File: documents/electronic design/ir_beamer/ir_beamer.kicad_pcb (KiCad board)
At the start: 2 copper layers, 140 parts, among them U1 74HC595D, U2 STM32F103HEADER, U3 74HC595D, U4 SE8R01_module

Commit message: update beamere pcb - MR_TOT in shift register, pull down
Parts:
- removed the C1 at (258.0, 110.3)
- removed the C1 at (233.8, 110.4)
- removed the C1 at (153.8, 110.4)
- removed the C1 at (179.3, 110.3)
- removed the C1 at (99.3, 110.3)
- removed the C1 at (73.8, 110.4)
- removed the C2 at (256.5, 25.0)
- removed the C2 at (235.4, 25.0)
- removed the C2 at (155.4, 25.0)
- removed the C2 at (177.7, 25.0)
- removed the C2 at (97.7, 25.0)
- removed the C2 at (75.4, 25.0)
- removed the C3 at (273.0, 38.2)
- removed the C3 at (218.8, 38.3)
- removed the C3 at (138.8, 38.3)
- removed the C3 at (194.3, 38.2)
- removed the C3 at (114.3, 38.2)
- removed the C3 at (58.8, 38.3)
- removed the D1 at (254.1, 74.0)
- removed the D1 at (237.7, 74.1)
- removed the D1 at (157.7, 74.1)
- removed the D1 at (175.4, 74.0)
- removed the D1 at (95.4, 74.0)
- removed the D1 at (77.7, 74.1)
- removed the D10 at (254.1, 61.3)
- removed the D10 at (237.7, 61.4)
- removed the D10 at (157.7, 61.4)
- removed the D10 at (175.4, 61.3)
- removed the D10 at (95.4, 61.3)
- removed the D10 at (77.7, 61.4)
- removed the D11 at (254.1, 67.6)
- removed the D11 at (237.7, 67.7)
- removed the D11 at (157.7, 67.7)
- removed the D11 at (175.4, 67.6)
- removed the D11 at (95.4, 67.6)
- removed the D11 at (77.7, 67.7)
- removed the D2 at (254.1, 42.2)
- removed the D2 at (237.7, 42.3)
- removed the D2 at (157.7, 42.3)
- removed the D2 at (175.4, 42.2)
- removed the D2 at (95.4, 42.2)
- removed the D2 at (77.7, 42.3)
- removed the D3 at (254.1, 80.3)
- removed the D3 at (237.7, 80.4)
- removed the D3 at (157.7, 80.4)
- removed the D3 at (175.4, 80.3)
- removed the D3 at (95.4, 80.3)
- removed the D3 at (77.7, 80.4)
- removed the D4 at (254.1, 86.7)
- removed the D4 at (237.7, 86.8)
- removed the D4 at (157.7, 86.8)
- removed the D4 at (175.4, 86.7)
- removed the D4 at (95.4, 86.7)
- removed the D4 at (77.7, 86.8)
- removed the D5 at (254.1, 93.0)
- removed the D5 at (237.7, 93.1)
- removed the D5 at (157.7, 93.1)
- removed the D5 at (175.4, 93.0)
- removed the D5 at (95.4, 93.0)
- removed the D5 at (77.7, 93.1)
- removed the D6 at (254.1, 99.4)
- removed the D6 at (237.7, 99.5)
- removed the D6 at (157.7, 99.5)
- removed the D6 at (175.4, 99.4)
- removed the D6 at (95.4, 99.4)
- removed the D6 at (77.7, 99.5)
- removed the D7 at (254.1, 105.7)
- removed the D7 at (237.7, 105.8)
- removed the D7 at (157.7, 105.8)
- removed the D7 at (175.4, 105.7)
- removed the D7 at (95.4, 105.7)
- removed the D7 at (77.7, 105.8)
- removed the D8 at (254.1, 48.6)
- removed the D8 at (237.7, 48.7)
- removed the D8 at (157.7, 48.7)
- removed the D8 at (175.4, 48.6)
- removed the D8 at (95.4, 48.6)
- removed the D8 at (77.7, 48.7)
- removed the D9 at (254.1, 54.9)
- removed the D9 at (237.7, 55.0)
- removed the D9 at (157.7, 55.0)
- removed the D9 at (175.4, 54.9)
- removed the D9 at (95.4, 54.9)
- removed the D9 at (77.7, 55.0)
- removed the R1 at (253.3, 111.1)
- removed the R1 at (238.6, 111.2)
- removed the R1 at (158.6, 111.2)
- removed the R1 at (174.5, 111.1)
- removed the R1 at (94.5, 111.1)
- removed the R1 at (78.6, 111.2)
- removed the R5 at (268.2, 86.4)
- removed the R5 at (223.7, 86.5)
- removed the R5 at (143.7, 86.5)
- removed the R5 at (189.4, 86.4)
- removed the R5 at (109.4, 86.4)
- removed the R5 at (63.7, 86.5)
- removed the U1 at (265.2, 105.0)
- removed the U1 at (226.6, 105.1)
- removed the U1 at (146.6, 105.1)
- removed the U1 at (186.4, 105.0)
- removed the U1 at (106.4, 105.0)
- removed the U1 at (66.6, 105.1)
- removed the U2 at (278.1, 96.7)
- removed the U2 at (213.7, 96.8)
- removed the U2 at (133.7, 96.8)
- removed the U2 at (199.4, 96.7)
- removed the U2 at (119.4, 96.7)
- removed the U2 at (53.7, 96.8)
- removed the U3 at (265.2, 40.2)
- removed the U3 at (226.6, 40.3)
- removed the U3 at (146.6, 40.3)
- removed the U3 at (186.4, 40.2)
- removed the U3 at (106.4, 40.2)
- removed the U3 at (66.6, 40.3)
- removed the U4 at (260.3, 22.4)
- removed the U4 at (231.5, 22.5)
- removed the U4 at (151.5, 22.5)
- removed the U4 at (181.6, 22.4)
- removed the U4 at (101.6, 22.4)
- removed the U4 at (71.5, 22.5)
- removed the U4 at (21.6, 22.4)
- added R2: 10K, Capacitors_SMD:C_0805_HandSoldering, F.Cu at (37.2, 38.8)
- added U4: SE8R01_module, footprints:SE8R01, F.Cu at (123.0, 23.5)
- moved C2 102.9 mm to (120.5, 19.6), turned to 270 degrees
- moved R1 96.8 mm to (34.3, 16.4), turned to 180 degrees
- moved D7 91.7 mm to (39.7, 17.3), turned to 270 degrees
- moved D2 91.3 mm to (103.2, 17.3), turned to 270 degrees
- moved C1 90.5 mm to (35.1, 21.2), turned to 90 degrees
- moved D6 87.6 mm to (46.0, 17.3), turned to 270 degrees
- moved D8 87.3 mm to (96.8, 17.3), turned to 270 degrees
- moved D5 84.3 mm to (52.4, 17.3), turned to 270 degrees
- moved D9 84.0 mm to (90.5, 17.3), turned to 270 degrees
- moved D4 81.8 mm to (58.7, 17.3), turned to 270 degrees
- moved D10 81.6 mm to (84.1, 17.3), turned to 270 degrees
- moved D3 80.3 mm to (65.1, 17.3), turned to 270 degrees
- moved D11 80.2 mm to (77.8, 17.3), turned to 270 degrees
- moved D1 79.7 mm to (71.4, 17.3), turned to 270 degrees
- moved U3 79.6 mm to (105.2, 28.3), turned to 180 degrees
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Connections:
- U1 pad 10: MR_NOT -> /MR_NOT
- U2 pad 11: MR_NOT -> (no net)
- U3 pad 10: MR_NOT -> /MR_NOT
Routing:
- net GND: track 1226.9 -> 179.2 mm, vias 42 -> 7
- net +3V3: track 1215.1 -> 173.6 mm, vias 35 -> 5
- net SPI_SCK: track 793.6 -> 113.4 mm, vias 42 -> 6
- net SPI_MOSI: track 642.8 -> 91.8 mm, vias 28 -> 4
- net MR_NOT: track 543.1 -> 0.00 mm, vias 14 -> 0
- net IR_PWM: track 588.1 -> 84.0 mm, vias 21 -> 3
- net Cascade: track 542.1 -> 77.4 mm
- net Latch: track 537.0 -> 77.5 mm, vias 14 -> 2
- net IR_GND: track 476.0 -> 68.0 mm
- net RADIO_CE: track 470.4 -> 67.2 mm
- net RADIO_CSN: track 437.7 -> 62.5 mm
- net RADIO_IRQ: track 435.4 -> 62.2 mm, vias 14 -> 2
- net SPI_MISO: track 355.2 -> 50.7 mm, vias 14 -> 2
- net IR_LED_2: track 216.1 -> 30.9 mm
- net IR_LED_DATA: track 190.4 -> 27.2 mm
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
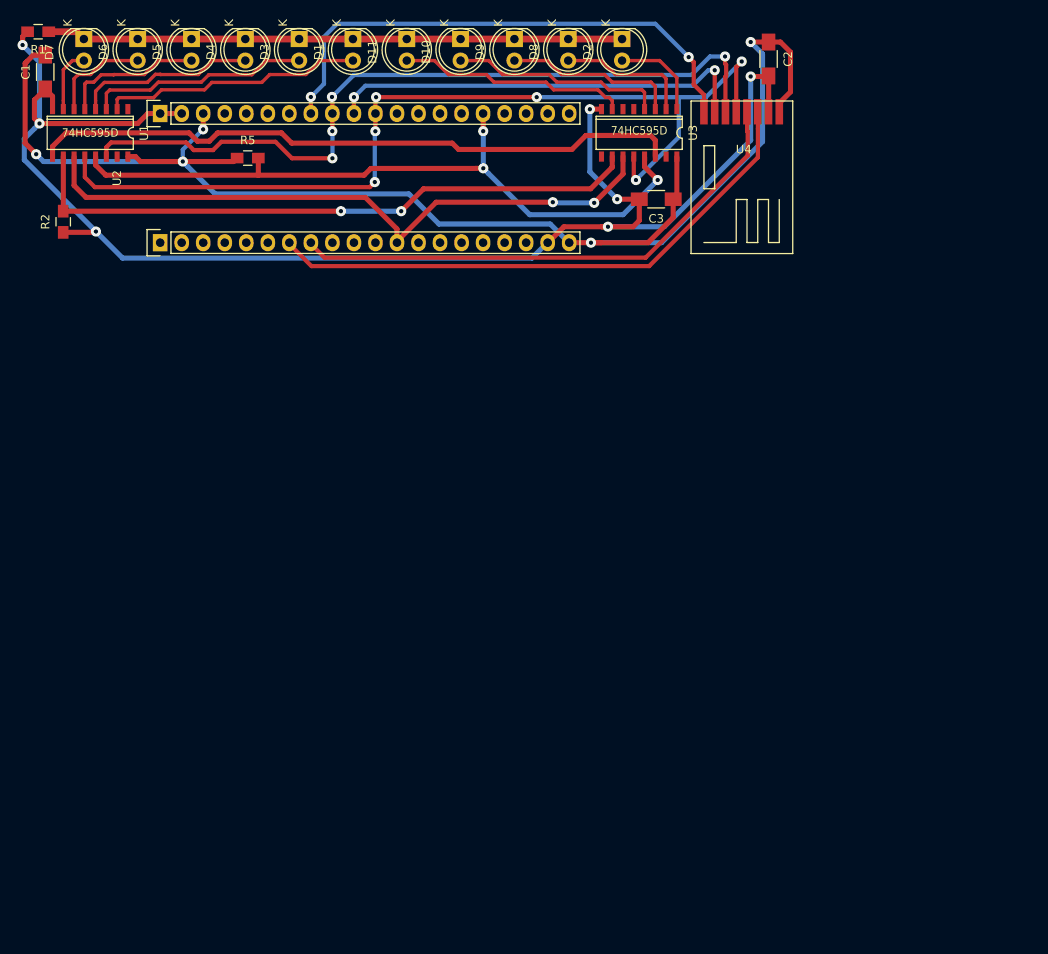
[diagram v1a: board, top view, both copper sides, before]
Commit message: pcb for beamer:  MR_NOT with pull down; radio; compact size
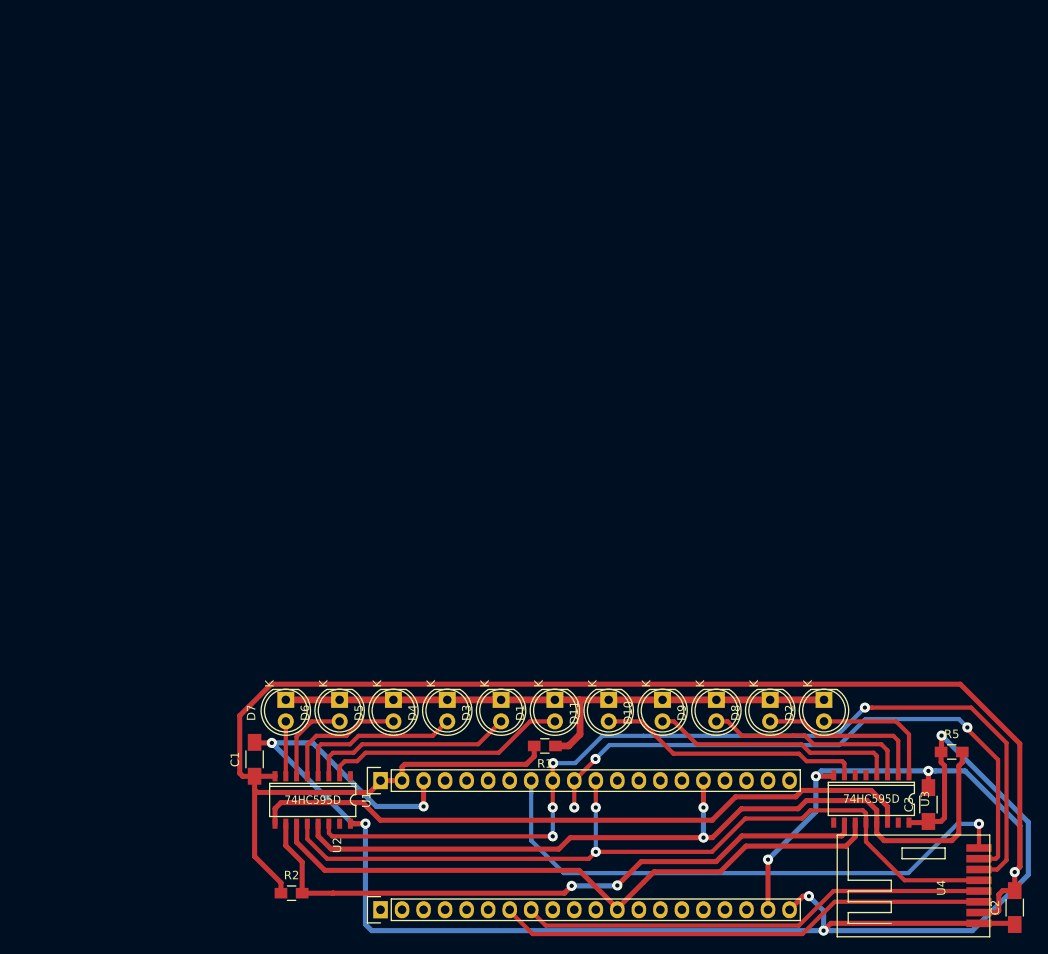
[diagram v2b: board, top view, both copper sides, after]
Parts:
- moved R5 108.7 mm to (142.1, 101.4)
- moved C2 104.2 mm to (149.5, 119.8), turned to 90 degrees
- moved R1 103.3 mm to (94.1, 100.7)
- moved U4 102.4 mm to (147.6, 122.9), turned to 90 degrees
- moved C1 84.8 mm to (59.8, 102.3)
- moved R2 83.7 mm to (64.2, 118.1), turned to 0 degrees
- moved U3 83.2 mm to (132.6, 106.9)
- moved U1 83.0 mm to (66.7, 107.1)
- moved U2 82.9 mm to (74.7, 120.0)
- moved D1 81.5 mm to (95.2, 95.2)
- moved D10 81.5 mm to (108.0, 95.2)
- moved D11 81.5 mm to (101.6, 95.2)
- moved D2 81.5 mm to (127.0, 95.2)
- moved D3 81.5 mm to (88.9, 95.2)
- moved D4 81.5 mm to (82.5, 95.2)
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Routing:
- net GND: track 179.2 -> 238.9 mm, vias 7 -> 4
- net +3V3: track 173.6 -> 201.7 mm, vias 5 -> 6
- net SPI_MISO: track 50.7 -> 72.2 mm, vias 2 -> 3
- net SPI_MOSI: track 91.8 -> 111.8 mm
- net IR_PWM: track 84.0 -> 100.5 mm, vias 3 -> 2
- net SPI_SCK: track 113.4 -> 98.2 mm, vias 6 -> 2
- net RADIO_CE: track 67.2 -> 58.2 mm
- net RADIO_CSN: track 62.5 -> 55.4 mm
- net RADIO_IRQ: track 62.2 -> 66.8 mm, vias 2 -> 1
- net IR_LED_1: track 11.0 -> 15.5 mm
- net IR_LED_8: track 16.0 -> 20.1 mm
- net IR_LED_DATA: track 27.2 -> 31.3 mm
- net IR_LED_9: track 20.6 -> 24.6 mm
- net IR_LED_10: track 25.2 -> 29.2 mm
- net IR_GND: track 68.0 -> 71.1 mm
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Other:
- net class Default: clearance 0.5 -> 0.6
- net class IR_SIGNAL: trace_width 0.4 -> 0.5
- net class POWER added: clearance 0.4, trace_width 0.6, via_dia 1.2, via_drill 0.5
- rule trace_clearance: 0.5 -> 0.6

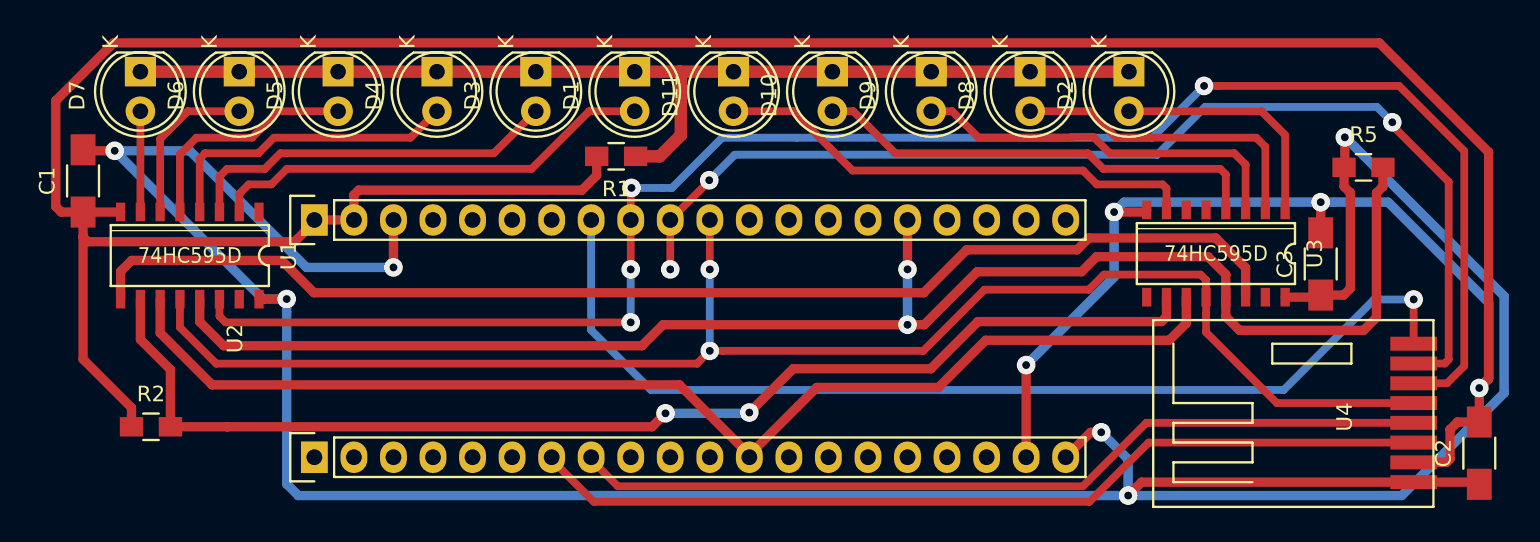
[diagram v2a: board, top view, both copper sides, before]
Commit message: fix mistake with pull up/ and down resistors in beamer pcb
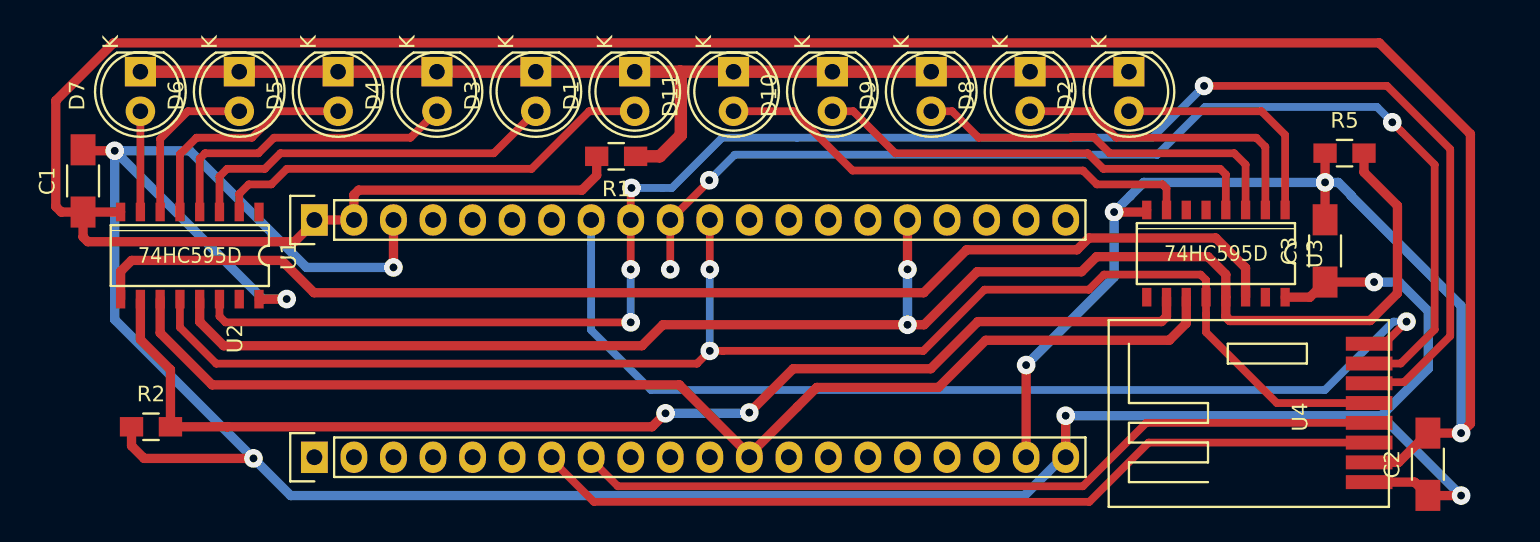
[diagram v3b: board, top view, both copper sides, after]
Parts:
- moved C2 3.38 mm to (146.2, 120.5)
- moved U4 2.86 mm to (144.8, 122.9)
- moved R5 1.52 mm to (140.8, 100.5)
- moved C3 0.88 mm to (139.6, 106.8)
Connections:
- R2 pad 1: GND -> +3V3
- R5 pad 1: +3V3 -> GND
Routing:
- net +3V3: track 201.7 -> 187.3 mm, vias 6 -> 7
- net GND: track 238.9 -> 230.1 mm
- net SPI_SCK: track 98.2 -> 95.3 mm
- net RADIO_CSN: track 55.4 -> 52.5 mm
- net RADIO_CE: track 58.2 -> 55.4 mm
- net IR_PWM: track 100.5 -> 102.0 mm
- net RADIO_IRQ: track 66.8 -> 65.9 mm
- net SPI_MISO: track 72.2 -> 72.9 mm

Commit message: update pcb
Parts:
- C1: value 100uf -> 100nf; footprint Capacitors_SMD:C_1206_HandSoldering -> Capacitors_SMD:C_0603_HandSoldering
- moved C2 156.2 mm to (19.5, 29.1), turned to 270 degrees
- moved C3 85.3 mm to (99.2, 31.6)
- moved R5 84.9 mm to (99.9, 26.1)
- moved D1 83.5 mm to (54.9, 22.1)
- moved D10 83.5 mm to (67.6, 22.1)
- moved D11 83.5 mm to (61.3, 22.1)
- moved D2 83.5 mm to (86.7, 22.1)
- moved D3 83.5 mm to (48.6, 22.1)
- moved D4 83.5 mm to (42.2, 22.1)
- moved D5 83.5 mm to (35.9, 22.1)
- moved D6 83.5 mm to (29.5, 22.1)
- moved D7 83.5 mm to (23.2, 22.1)
- moved D8 83.5 mm to (80.3, 22.1)
- moved D9 83.5 mm to (74.0, 22.1)
- moved R1 83.5 mm to (53.8, 27.5)
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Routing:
- net +3V3: track 187.3 -> 312.7 mm
- net GND: track 230.1 -> 176.5 mm
- net /MR_NOT: track 77.2 -> 71.8 mm, vias 2 -> 0
- net (no net): track 0.00 -> 5.41 mm, vias 0 -> 2
- net IR_PWM: track 102.0 -> 101.0 mm
- net SPI_MISO: track 72.9 -> 72.0 mm
- net SPI_MOSI: track 111.8 -> 110.9 mm
- net RADIO_IRQ: track 65.9 -> 66.6 mm

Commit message: update pcb for beamer
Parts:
- removed U2: STM32F103HEADER, footprints:STM32F103_header_footprint
- added P1: CONN_02X05, Pin_Headers:Pin_Header_Straight_2x05, F.Cu at (189.7, 92.4)
- C1: value 100nf -> 100uf
- moved D7 166.1 mm to (179.8, 77.5)
- moved C2 148.6 mm to (156.6, 86.6), turned to 90 degrees
- moved D2 95.9 mm to (165.0, 77.5)
- moved R1 91.1 mm to (122.4, 87.5), turned to 0 degrees
- moved D8 89.0 mm to (150.0, 77.5)
- moved D11 83.1 mm to (112.5, 87.5)
- moved D9 82.4 mm to (135.0, 77.5)
- moved U3 77.8 mm to (149.4, 86.6)
- moved D10 76.2 mm to (120.0, 77.5)
- moved D1 74.7 mm to (105.0, 77.5)
- moved C3 70.3 mm to (55.1, 86.4)
- moved U4 68.9 mm to (165.2, 82.3), turned to 270 degrees
- moved C1 68.9 mm to (163.4, 84.7), turned to 90 degrees
- moved D3 68.5 mm to (88.9, 77.5)
- moved R5 67.1 mm to (127.6, 87.2), turned to 90 degrees
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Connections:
- U1 pad 2: IR_LED_2 -> (no net)
- U1 pad 3: IR_LED_3 -> IR_LED_2
- U1 pad 4: IR_LED_4 -> IR_LED_3
- U1 pad 5: IR_LED_5 -> IR_LED_4
- U1 pad 6: IR_LED_6 -> IR_LED_5
- U1 pad 7: IR_LED_7 -> IR_LED_6
- U3 pad 1: IR_LED_1 -> IR_LED_DATA
- U3 pad 2: IR_LED_8 -> IR_LED_7
- U3 pad 3: IR_LED_9 -> IR_LED_1
- U3 pad 4: IR_LED_10 -> IR_LED_8
- U3 pad 5: (no net) -> IR_LED_9
- U3 pad 6: (no net) -> IR_LED_10
- U3 pad 7: IR_LED_DATA -> (no net)
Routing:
- net +3V3: track 312.7 -> 204.2 mm, vias 7 -> 5
- net IR_GND: track 71.1 -> 153.5 mm, vias 0 -> 2
- net Latch: track 76.7 -> 157.8 mm, vias 0 -> 4
- net GND: track 176.5 -> 254.7 mm, vias 4 -> 6
- net SPI_SCK: track 95.3 -> 155.2 mm, vias 2 -> 3
- net IR_PWM: track 101.0 -> 159.2 mm, vias 2 -> 1
- net SPI_MISO: track 72.0 -> 21.2 mm, vias 3 -> 0
- net RADIO_IRQ: track 66.6 -> 19.6 mm, vias 1 -> 0
- net IR_LED_DATA: track 31.3 -> 63.7 mm, vias 0 -> 2
- net Cascade: track 79.3 -> 103.9 mm
- net IR_LED_7: track 6.22 -> 29.9 mm
- net SPI_MOSI: track 110.9 -> 133.3 mm, vias 4 -> 5
- net /MR_NOT: track 71.8 -> 93.5 mm
- net IR_LED_8: track 20.1 -> 3.80 mm
- net IR_LED_2: track 28.8 -> 43.4 mm
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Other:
- net class Default: clearance 0.6 -> 0.3; trace_width 0.6 -> 0.4
- net class IR_SIGNAL: trace_width 0.5 -> 0.4
- net class RADIO: trace_width 0.5 -> 0.4
- rule trace_clearance: 0.6 -> 0.3
